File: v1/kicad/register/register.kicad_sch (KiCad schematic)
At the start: 5 parts, among them J3 ASYNC_{out}, U1 74HC173, U2 74HC173, U3 74LS244, U5 LNCPU Type B Connector

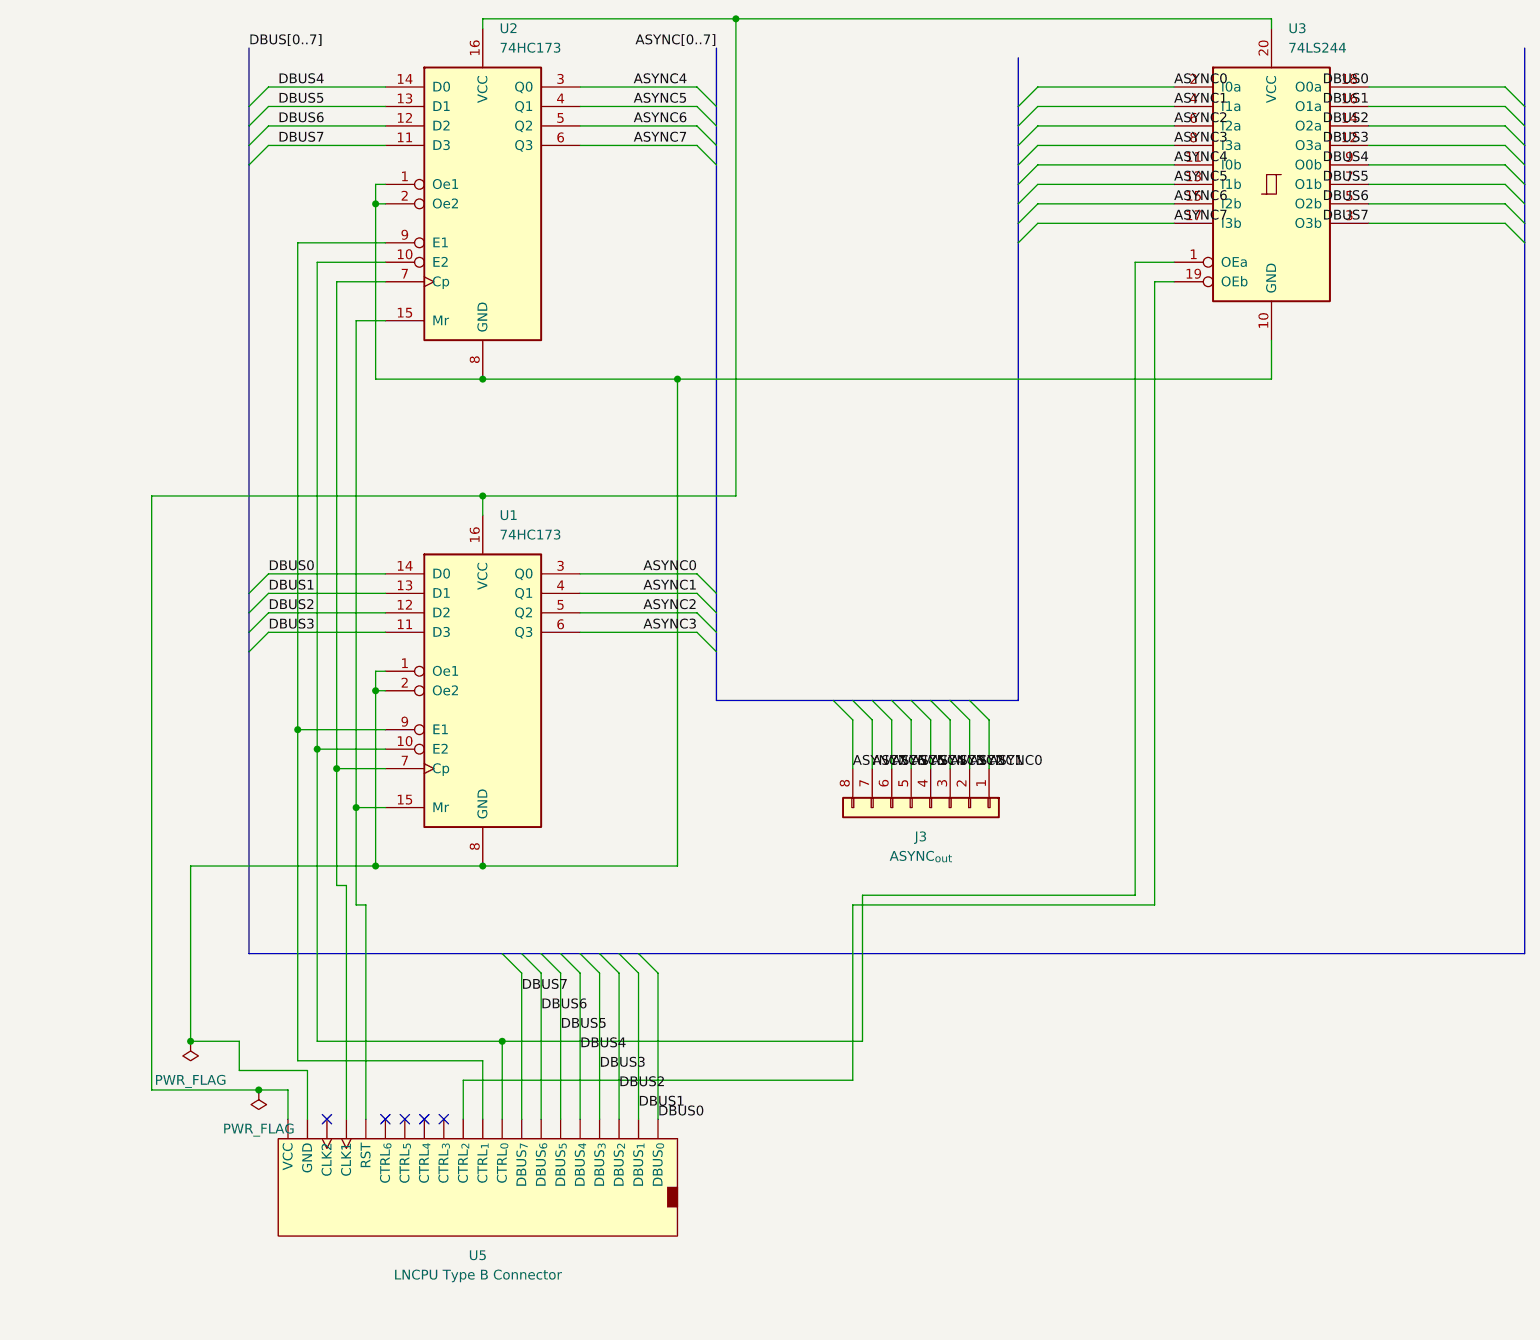
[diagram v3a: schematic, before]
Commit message: check designs for ALU (partial), SP, Shift register, register
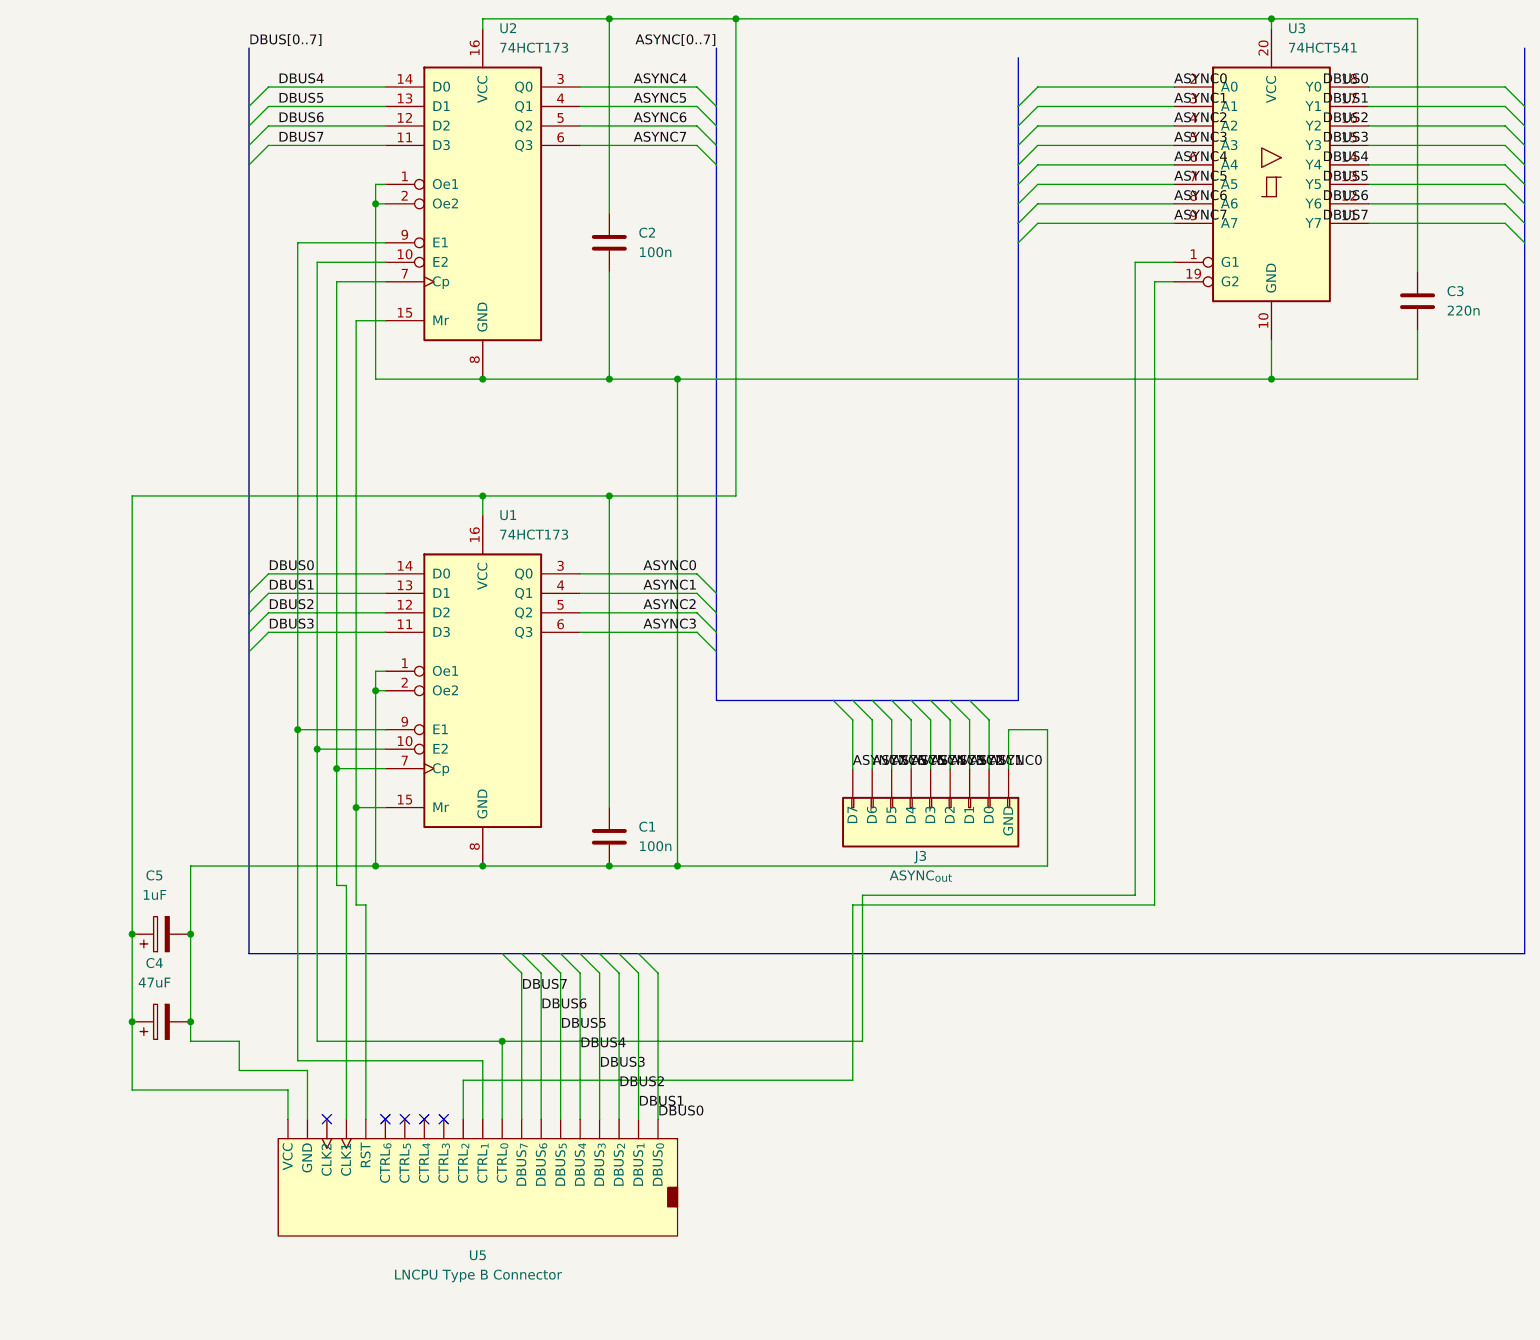
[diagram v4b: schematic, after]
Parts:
- removed U1, U2: 74HC173, Package_DIP:DIP-16_W7.62mm_LongPads, symbol 74xx:74HC173
- removed U3: 74LS244, Package_DIP:DIP-20_W7.62mm_LongPads, symbol 74xx:74LS244
- added C1, C2: 100n, Capacitor_THT:C_Disc_D4.3mm_W1.9mm_P5.00mm, symbol Device:C
- added C3: 220n, Capacitor_THT:C_Disc_D4.3mm_W1.9mm_P5.00mm, symbol Device:C
- added C4: 47uF, Capacitor_THT:CP_Radial_D5.0mm_P2.50mm, symbol Device:C_Polarized
- added C5: 1uF, lncpu:CP_Radial_D4.0mm_P2.00mm-Large-Holes, symbol Device:C_Polarized
- added U1, U2: 74HCT173, Package_DIP:DIP-16_W7.62mm_LongPads, symbol 74xx:74HCT173
- added U3: 74HCT541, Package_DIP:DIP-20_W7.62mm_LongPads, symbol 74xx:74HCT541
- J3: footprint Connector_PinSocket_2.54mm:PinSocket_1x08_P2.54mm_Vertical -> Connector_PinSocket_2.54mm:PinSocket_1x10_P2.54mm_Vertical; symbol Connector_Generic:Conn_01x08 -> lncpu:LNCPU_8B_Socket
- U5: symbol lncpu:LNCPU_Type_B_Connector -> lncpu:LNCPU_Type_B_Header
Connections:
- net ASYNC0: now also J3.2 (D0), U1.3 (Q0), U3.2 (A0); no longer J3.1 (Pin_1)
- net ASYNC1: now also J3.3 (D1), U1.4 (Q1), U3.3 (A1); no longer J3.2 (Pin_2)
- net ASYNC2: now also J3.4 (D2), U1.5 (Q2), U3.4 (A2); no longer J3.3 (Pin_3)
- net ASYNC3: now also J3.5 (D3), U1.6 (Q3), U3.5 (A3); no longer J3.4 (Pin_4)
- net ASYNC4: now also J3.6 (D4), U2.3 (Q0), U3.6 (A4); no longer J3.5 (Pin_5)
- net ASYNC5: now also J3.7 (D5), U2.4 (Q1), U3.7 (A5); no longer J3.6 (Pin_6)
- net ASYNC6: now also J3.8 (D6), U2.5 (Q2), U3.8 (A6); no longer J3.7 (Pin_7)
- net ASYNC7: now also J3.9 (D7), U2.6 (Q3), U3.9 (A7); no longer J3.8 (Pin_8)
- net DBUS0: now also U1.14 (D0), U3.18 (Y0)
- net DBUS1: now also U1.13 (D1), U3.17 (Y1)
- net DBUS2: now also U1.12 (D2), U3.16 (Y2)
- net DBUS3: now also U1.11 (D3), U3.15 (Y3)
- net DBUS4: now also U2.14 (D0), U3.14 (Y4)
- net DBUS5: now also U2.13 (D1), U3.13 (Y5)
- net DBUS6: now also U2.12 (D2), U3.12 (Y6)
- net DBUS7: now also U2.11 (D3), U3.11 (Y7)
- net at U5.1 (GND), U5.17 (GND), U5.20 (GND)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: now also J3.1 (GND), J3.10 (GND), C1.2, C2.2, C3.2, C4.2, C5.2, U1.1 (Oe1), U1.2 (Oe2), U1.8 (GND), U2.1 (Oe1), U2.2 (Oe2), U2.8 (GND), U3.10 (GND)
- net at U5.3 (CTRL_{0}): now also U1.10 (E2), U2.10 (E2), U3.1 (G1)
- net at U5.19 (RST): now also U1.15 (Mr), U2.15 (Mr)
- net at U5.2 (VCC), U5.24 (VCC): now also C1.1, C2.1, C3.1, C4.1, C5.1, U1.16 (VCC), U2.16 (VCC), U3.20 (VCC)
- net at U5.21 (CLK1): now also U1.7 (Cp), U2.7 (Cp)
- net at U5.5 (CTRL_{1}): now also U1.9 (E1), U2.9 (E1)
- net at U5.7 (CTRL_{2}): now also U3.19 (G2)

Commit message: readapt designs for BR, SP, SR, ALU
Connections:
- net DBUS0: now also U5.3 (DBUS_{0}); no longer U5.4 (DBUS_{0})
- net DBUS1: now also U5.5 (DBUS_{1}); no longer U5.6 (DBUS_{1})
- net DBUS2: now also U5.7 (DBUS_{2}); no longer U5.8 (DBUS_{2})
- net DBUS3: now also U5.9 (DBUS_{3}); no longer U5.10 (DBUS_{3})
- net DBUS4: now also U5.11 (DBUS_{4}); no longer U5.12 (DBUS_{4})
- net DBUS5: now also U5.13 (DBUS_{5}); no longer U5.14 (DBUS_{5})
- net DBUS6: now also U5.15 (DBUS_{6}); no longer U5.16 (DBUS_{6})
- net DBUS7: now also U5.17 (DBUS_{7}); no longer U5.18 (DBUS_{7})
- net at C1.1, C2.1, C3.1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: now also J3.10 (VCC)
- net at C1.2, C2.2, C3.2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: now also U5.18 (GND), U5.23 (GND); no longer J3.10 (GND), U5.17 (GND), U5.20 (GND)
- net at U1.10 (E2), U2.10 (E2), U3.1 (G1): now also U5.4 (CTRL_{0}); no longer U5.3 (CTRL_{0})
- net at U1.9 (E1), U2.9 (E1): now also U5.6 (CTRL_{1}); no longer U5.5 (CTRL_{1})
- net at U3.19 (G2): now also U5.8 (CTRL_{2}); no longer U5.7 (CTRL_{2})
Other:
- moved on the sheet: U5
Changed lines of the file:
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@@
+	)
+	(junction
+		(at 128.27 82.55)
+		(diameter 0)
+		(color 0 0 0 0)
 	)
 	(junction
@@
 	(wire
 		(pts
+			(xy 137.16 82.55) (xy 137.16 118.11)
+		)
+		(stroke
+			(width 0)
+			(type default)
+		)
+	)
+	(wire
+		(pts
 			(xy 81.28 44.45) (xy 82.55 44.45)
 		)
@@
 	(wire
 		(pts
+			(xy 137.16 118.11) (xy 140.97 118.11)
+		)
+		(stroke
+			(width 0)
+			(type default)
+		)
+	)
+	(wire
+		(pts
 			(xy 67.31 92.71) (xy 82.55 92.71)
 		)
@@
 		)
 		(stroke
+			(width 0)
+			(type default)
+		)
+	)
+	(wire
+		(pts
+			(xy 128.27 82.55) (xy 137.16 82.55)
+		)
+		(stroke
